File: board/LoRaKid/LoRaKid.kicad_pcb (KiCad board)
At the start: 2 copper layers, 100 x 120 mm, 15 parts, among them Q1 NPN, SW1_ON_OFF1 SW_Push, SW2_LEFT1 SW_Push, SW3_RIGHT1 SW_Push, SW4 SW_Push, SW5 SW_Push, SW6 SW_Push, SW7 SW_Push, SW8 SW_Push, SW9 SW_Push

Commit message: update board layout
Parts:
- added BAT1: Conn_01x02_Pin, Connector_JST:JST_PH_B2B-PH-K_1x02_P2.00mm_Vertical, F.Cu at (149.0, 119.5)
- added J1: Conn_01x02_Pin, Connector_PinHeader_2.54mm:PinHeader_1x02_P2.54mm_Vertical, F.Cu at (134.7, 121.5)
- added REF1: MountingHole_2.2mm_M2, MountingHole:MountingHole_2.2mm_M2, F.Cu at (105.0, 139.5)
- added REF2: MountingHole_2.2mm_M2, MountingHole:MountingHole_2.2mm_M2, F.Cu at (165.5, 139.5)
- added REF3: MountingHole_2.2mm_M2, MountingHole:MountingHole_2.2mm_M2, F.Cu at (105.0, 29.5)
- added REF4: MountingHole_2.2mm_M2, MountingHole:MountingHole_2.2mm_M2, F.Cu at (165.5, 29.5)
- R1, R2: footprint Resistor_SMD:R_0805_2012Metric_Pad1.20x1.40mm_HandSolder -> Resistor_SMD:R_1206_3216Metric_Pad1.30x1.75mm_HandSolder
- moved R2 101.9 mm to (116.1, 122.5)
- moved R1 94.5 mm to (124.5, 122.5)
- moved Q1 84.1 mm to (118.8, 113.0)
- moved SW3_RIGHT1 38.5 mm to (151.0, 36.0)
- moved USB1 35.8 mm to (131.9, 132.5)
- moved SW2_LEFT1 35.0 mm to (121.0, 36.0)
- moved SW1_ON_OFF1 10.7 mm to (107.2, 36.0)
- moved SW6 4.52 mm to (155.5, 81.3)
- moved SW9 4.52 mm to (155.5, 99.1)
- moved SW4 4.52 mm to (114.9, 81.3)
- moved SW7 4.52 mm to (114.9, 99.1)
- moved SW5 4.52 mm to (135.2, 81.3)
- moved SW8 4.52 mm to (135.2, 99.1)
- moved BZ1 2.50 mm to (132.7, 36.0)
- moved U1 1.40 mm to (129.4, 58.4)
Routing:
- net Net-(BZ1--): track 26.7 -> 241.2 mm
- net Net-(U1-GPIO38): track 164.7 -> 60.8 mm
- net Net-(U1-GPIO39): track 0.00 -> 68.8 mm, vias 0 -> 1
- net Net-(U1-GPIO26): track 0.00 -> 61.4 mm
- net Net-(U1-GPIO47): track 0.00 -> 59.3 mm
- net Net-(U1-GPIO40): track 0.00 -> 57.8 mm, vias 0 -> 1
- net Net-(U1-GPIO33): track 54.2 -> 91.1 mm
- net Net-(U1-GPIO48): track 0.00 -> 35.8 mm
- net Net-(U1-PROG): track 85.0 -> 54.9 mm, vias 0 -> 1
- net Net-(U1-GPIO6/ADC1_5): track 8.00 -> 28.6 mm
- net Net-(BAT1-Pin_2): track 0.00 -> 19.3 mm
- net Net-(Q1-B): track 22.7 -> 33.4 mm
- net Net-(U1-GPIO7/ADC1_6): track 66.3 -> 55.7 mm
- net +3.3V: track 36.1 -> 27.7 mm
- net Net-(U1-5V): track 62.2 -> 70.3 mm
- added copper zone on B.Cu, net GND
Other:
- board size 100 x 120 mm -> 69 x 120 mm

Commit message: update board design
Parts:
- Q1: footprint Package_TO_SOT_THT:TO-92_Inline -> Package_TO_SOT_THT:TO-92_HandSolder
- moved Q1 4.93 mm to (120.2, 108.3)
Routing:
- net Net-(BZ1--): track 241.2 -> 123.6 mm
- net Net-(U1-GPIO39): track 68.8 -> 114.0 mm
- net Net-(Q1-B): track 33.4 -> 61.8 mm
- net Net-(U1-GPIO40): track 57.8 -> 83.6 mm
- net Net-(U1-GPIO6/ADC1_5): track 28.6 -> 47.7 mm
- net Net-(U1-GPIO7/ADC1_6): track 55.7 -> 69.2 mm
- net Net-(U1-GPIO26): track 61.4 -> 73.8 mm
- net Net-(U1-GPIO38): track 60.8 -> 69.0 mm
- net Net-(U1-PROG): track 54.9 -> 61.6 mm
- net Net-(U1-GPIO47): track 59.3 -> 63.7 mm
- net Net-(U1-GPIO33): track 91.1 -> 87.8 mm
- net +3.3V: track 27.7 -> 29.0 mm

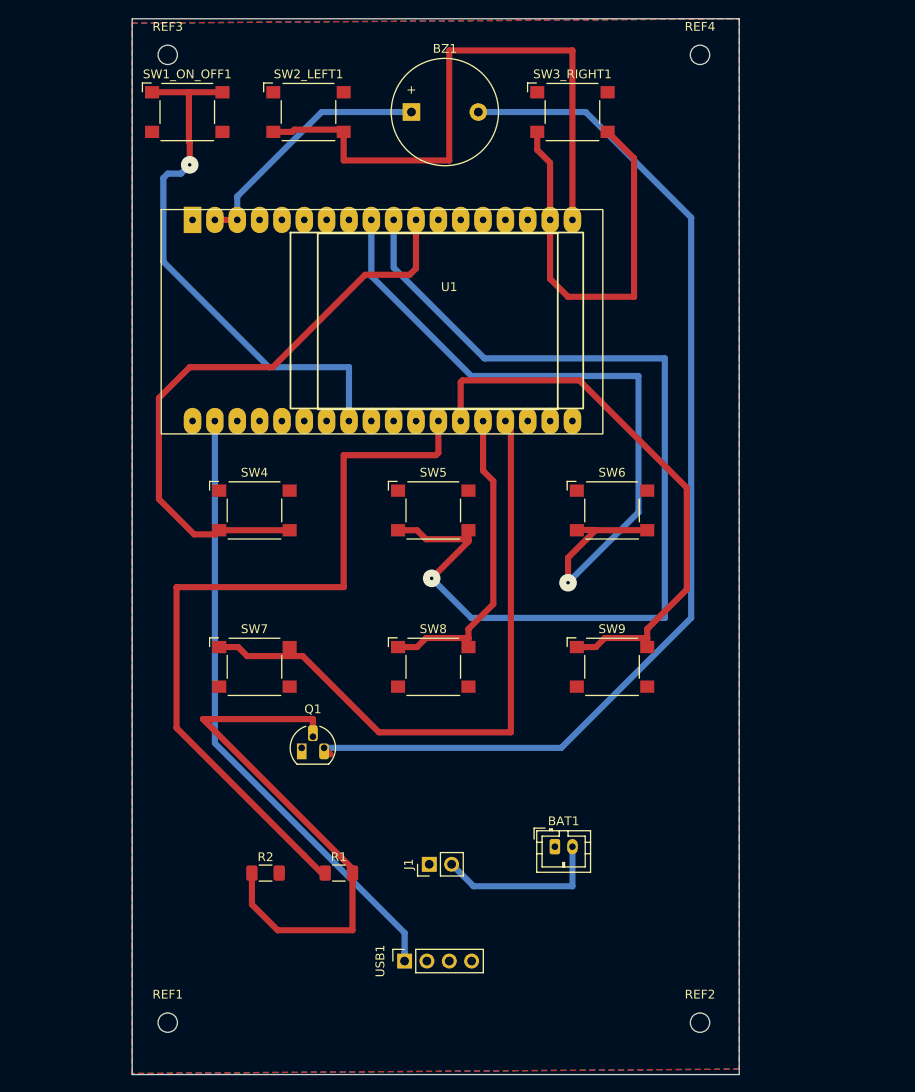
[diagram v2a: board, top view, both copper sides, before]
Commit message: update board layout and software
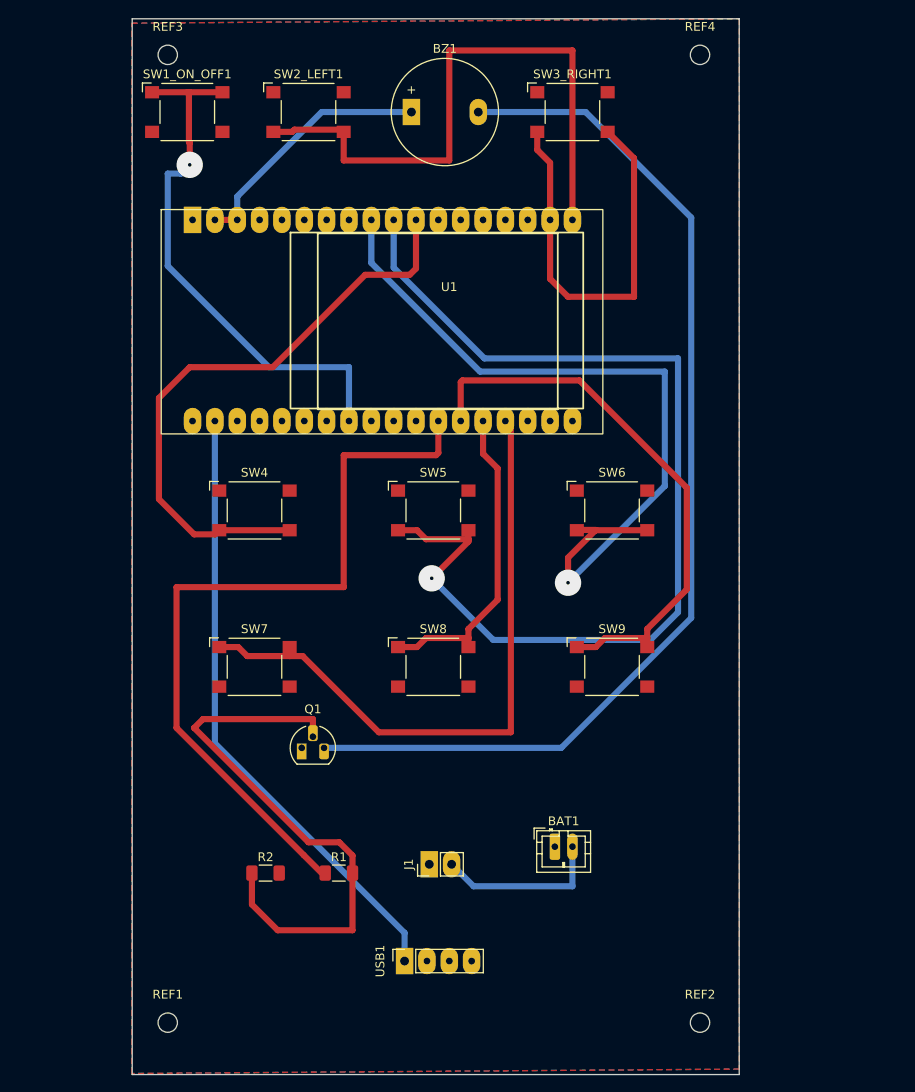
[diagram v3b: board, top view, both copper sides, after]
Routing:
- net Net-(U1-GPIO39): track 114.0 -> 118.7 mm
- net Net-(U1-GPIO40): track 83.6 -> 87.2 mm
- net Net-(Q1-B): track 61.8 -> 64.6 mm
- net Net-(BZ1--): track 123.6 -> 122.5 mm
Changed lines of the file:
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@@
 		(allow_soldermask_bridges_in_footprints no)
 		(pcbplotparams
-			(layerselection 0x000003c_7ffffffe)
-			(plot_on_all_layers_selection 0x0000000_00000000)
+			(layerselection 0x0000000_ffffffff)
+			(plot_on_all_layers_selection 0x0001000_00000000)
 			(disableapertmacros no)
 			(usegerberextensions no)
@@
 		)
 		(pad "1" thru_hole rect
-			(at 0 0 90)
-			(size 1.7 1.7)
+			(at 0 0 180)
+			(size 2 3)
 			(drill 1)
 			(layers "*.Cu" "*.Mask")
@@
 		)
 		(pad "2" thru_hole oval
-			(at 0 2.54 90)
-			(size 1.7 1.7)
-			(drill 1)
+			(at 0 2.54 180)
+			(size 2 3)
+			(drill 0.762)
 			(layers "*.Cu" "*.Mask")
 			(remove_unused_layers no)
@@
 		)
 		(pad "3" thru_hole oval
-			(at 0 5.08 90)
-			(size 1.7 1.7)
-			(drill 1)
+			(at 0 5.08 180)
+			(size 2 3)
+			(drill 0.762)
 			(layers "*.Cu" "*.Mask")
 			(remove_unused_layers no)
@@
 		)
 		(pad "4" thru_hole oval
-			(at 0 7.62 90)
-			(size 1.7 1.7)
-			(drill 1)
+			(at 0 7.62 180)
+			(size 2 3)
+			(drill 0.762)
 			(layers "*.Cu" "*.Mask")
 			(remove_unused_layers no)
@@
 		(pad "1" thru_hole roundrect
 			(at 0 0)
-			(size 1.2 1.75)
+			(size 1.2 3)
 			(drill 0.75)
 			(layers "*.Cu" "*.Mask")
@@
 		(pad "2" thru_hole oval
 			(at 2 0)
-			(size 1.2 1.75)
+			(size 1.2 3)
 			(drill 0.75)
 			(layers "*.Cu" "*.Mask")
@@
 		(pad "1" thru_hole rect
 			(at 0 0)
-			(size 2 2)
+			(size 2 3)
 			(drill 1)
 			(layers "*.Cu" "*.Mask")
@@
 			(pintype "passive")
 		)
-		(pad "2" thru_hole circle
+		(pad "2" thru_hole oval
 			(at 7.6 0)
-			(size 2 2)
+			(size 2 3)
 			(drill 1)
 			(layers "*.Cu" "*.Mask")
@@
 		)
 		(pad "1" thru_hole rect
-			(at 0 0 90)
-			(size 1.7 1.7)
+			(at 0 0 180)
+			(size 2 3)
 			(drill 1)
 			(layers "*.Cu" "*.Mask")
@@
 		)
 		(pad "2" thru_hole oval
-			(at 0 2.54 90)
-			(size 1.7 1.7)
+			(at 0 2.54 180)
+			(size 2 3)
 			(drill 1)
 			(layers "*.Cu" "*.Mask")
@@
 	(via
 		(at 107.5 42)
-		(size 2)
+		(size 3)
 		(drill 0.4)
 		(layers "F.Cu" "B.Cu")
@@
 	)
 	(segment
-		(start 125.6 65)
-		(end 125.6 71.12)
+		(start 106.5 43)
+		(end 105 43)
 		(width 0.7)
 		(layer "B.Cu")
@@
 	)
 	(segment
-		(start 106.5 43)
-		(end 105 43)
+		(start 107.5 42)
+		(end 106.5 43)
 		(width 0.7)
 		(layer "B.Cu")
@@
 	)
 	(segment
-		(start 104.5 53)
+		(start 105 53.5)
 		(end 116.5 65)
 		(width 0.7)
@@
 	)
 	(segment
-		(start 104.5 43.5)
-		(end 104.5 53)
+		(start 125.6 65)
+		(end 125.6 71.12)
 		(width 0.7)
 		(layer "B.Cu")
@@
 	(segment
 		(start 105 43)
-		(end 104.5 43.5)
-		(width 0.7)
-		(layer "B.Cu")
-		(net 2)
-	)
-	(segment
-		(start 107.5 42)
-		(end 106.5 43)
+		(end 105 53.5)
 		(width 0.7)
 		(layer "B.Cu")
@@
 	(via
 		(at 135 89)
-		(size 2)
+		(size 3)
 		(drill 0.4)
 		(layers "F.Cu" "B.Cu")
@@
 	)
 	(segment
-		(start 139.5 93.5)
-		(end 161.5 93.5)
+		(start 163 63.9987)
+		(end 140.9987 63.9987)
 		(width 0.7)
 		(layer "B.Cu")
@@
 	)
 	(segment
-		(start 161.5 63.9987)
-		(end 140.9987 63.9987)
+		(start 142 96)
+		(end 159.863604 96)
 		(width 0.7)
 		(layer "B.Cu")
@@
 	)
 	(segment
-		(start 161.5 93.5)
-		(end 161.5 63.9987)
+		(start 130.68 53.68)
+		(end 130.68 48.26)
 		(width 0.7)
 		(layer "B.Cu")
@@
 	)
 	(segment
-		(start 140.9987 63.9987)
-		(end 130.68 53.68)
+		(start 163 92.863604)
+		(end 163 63.9987)
 		(width 0.7)
 		(layer "B.Cu")
@@
 	(segment
 		(start 135 89)
-		(end 139.5 93.5)
+		(end 142 96)
 		(width 0.7)
 		(layer "B.Cu")
@@
 	)
 	(segment
-		(start 130.68 53.68)
-		(end 130.68 48.26)
+		(start 140.9987 63.9987)
+		(end 130.68 53.68)
+		(width 0.7)
+		(layer "B.Cu")
+		(net 6)
+	)
+	(segment
+		(start 159.863604 96)
+		(end 163 92.863604)
 		(width 0.7)
 		(layer "B.Cu")
@@
 	(via
 		(at 150.5 89.5)
-		(size 2)
+		(size 3)
 		(drill 0.4)
 		(layers "F.Cu" "B.Cu")
@@
 	)
 	(segment
-		(start 139.5 66)
-		(end 128.14 54.64)
+		(start 161.5 65.5)
+		(end 140.5 65.5)
 		(width 0.7)
 		(layer "B.Cu")
@@
 	)
 	(segment
-		(start 150.5 89.5)
-		(end 158.5 81.5)
+		(start 128.14 53.14)
+		(end 128.14 48.26)
 		(width 0.7)
 		(layer "B.Cu")
@@
 	)
 	(segment
-		(start 158.5 81.5)
-		(end 158.5 66)
+		(start 150.5 89.5)
+		(end 161.5 78.5)
 		(width 0.7)
 		(layer "B.Cu")
@@
 	)
 	(segment
-		(start 158.5 66)
-		(end 139.5 66)
+		(start 140.5 65.5)
+		(end 128.14 53.14)
 		(width 0.7)
 		(layer "B.Cu")
@@
 	)
 	(segment
-		(start 128.14 54.64)
-		(end 128.14 48.26)
+		(start 161.5 78.5)
+		(end 161.5 65.5)
 		(width 0.7)
 		(layer "B.Cu")
@@
 	)
 	(segment
-		(start 131.18 96.81)
-		(end 133.332 96.81)
-		(width 0.7)
-		(layer "F.Cu")
-		(net 9)
-	)
-	(segment
-		(start 139.18 95.7841)
-		(end 139.18 96.81)
+		(start 139.18 94.7583)
+		(end 139.18 95.7841)
 		(width 0.7)
 		(layer "F.Cu")
@@
 	)
 	(segment
-		(start 142.004 91.934)
-		(end 139.18 94.7583)
+		(start 131.18 96.81)
+		(end 133.332 96.81)
 		(width 0.7)
 		(layer "F.Cu")
@@
 	)
 	(segment
-		(start 142.004 77.9326)
-		(end 142.004 91.934)
+		(start 139.18 95.7841)
+		(end 139.18 96.81)
 		(width 0.7)
 		(layer "F.Cu")
@@
 	)
 	(segment
-		(start 140.84 76.7683)
-		(end 142.004 77.9326)
+		(start 142.5 91.4383)
+		(end 139.18 94.7583)
 		(width 0.7)
 		(layer "F.Cu")
@@
 	)
 	(segment
-		(start 139.18 94.7583)
-		(end 139.18 95.7841)
+		(start 140.84 74.84)
+		(end 142.5 76.5)
 		(width 0.7)
 		(layer "F.Cu")
@@
 	(segment
 		(start 140.84 71.12)
-		(end 140.84 76.7683)
+		(end 140.84 74.84)
+		(width 0.7)
+		(layer "F.Cu")
+		(net 9)
+	)
+	(segment
+		(start 142.5 76.5)
+		(end 142.5 91.4383)
 		(width 0.7)
 		(layer "F.Cu")
@@
 	)
 	(segment
-		(start 123.5 109)
-		(end 122.77 108.27)
-		(width 0.7)
-		(layer "F.Cu")
-		(net 32)
-	)
-	(segment
 		(start 149.73 108.27)
 		(end 122.77 108.27)
@@
 	)
 	(segment
-		(start 109 105)
-		(end 121.5 105)
+		(start 121.5 105)
+		(end 121.5 107)
+		(width 0.7)
+		(layer "F.Cu")
+		(net 34)
+	)
+	(segment
+		(start 121 119)
+		(end 108 106)
 		(width 0.7)
 		(layer "F.Cu")
@@
 	)
 	(segment
-		(start 114.57 126.07)
-		(end 117.5 129)
+		(start 108 106)
+		(end 109 105)
 		(width 0.7)
 		(layer "F.Cu")
@@
 	)
 	(segment
-		(start 126 122)
-		(end 109 105)
+		(start 114.57 126.07)
+		(end 117.5 129)
 		(width 0.7)
 		(layer "F.Cu")
@@
 	)
 	(segment
-		(start 114.57 122.5)
-		(end 114.57 126.07)
+		(start 126 120.5)
+		(end 124.5 119)
+		(width 0.7)
+		(layer "F.Cu")
+		(net 34)
+	)
+	(segment
+		(start 109 105)
+		(end 121.5 105)
 		(width 0.7)
 		(layer "F.Cu")
@@
 	(segment
 		(start 126 122.5)
-		(end 126 122)
+		(end 126 120.5)
 		(width 0.7)
 		(layer "F.Cu")
@@
 	)
 	(segment
-		(start 121.5 105)
-		(end 121.5 107)
+		(start 114.57 122.5)
+		(end 114.57 126.07)
+		(width 0.7)
+		(layer "F.Cu")
+		(net 34)
+	)
+	(segment
+		(start 124.5 119)
+		(end 121 119)
 		(width 0.7)
 		(layer "F.Cu")
@@
 			(clearance 0.75)
 		)
-		(min_thickness 1)
+		(min_thickness 0.75)
 		(filled_areas_thickness no)
 		(fill yes
